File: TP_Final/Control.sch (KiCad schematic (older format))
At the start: 52 parts, among them J101 BG 1x2, J102 BD 1x2, J103 BG 1x2, J104 BG 1x3, J105 Poste 1x4, J106 Poste 2x4, J107 Poste 2x3, K101 EC2-3NU, K102 EC2-3NU, K103 EC2-3NU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

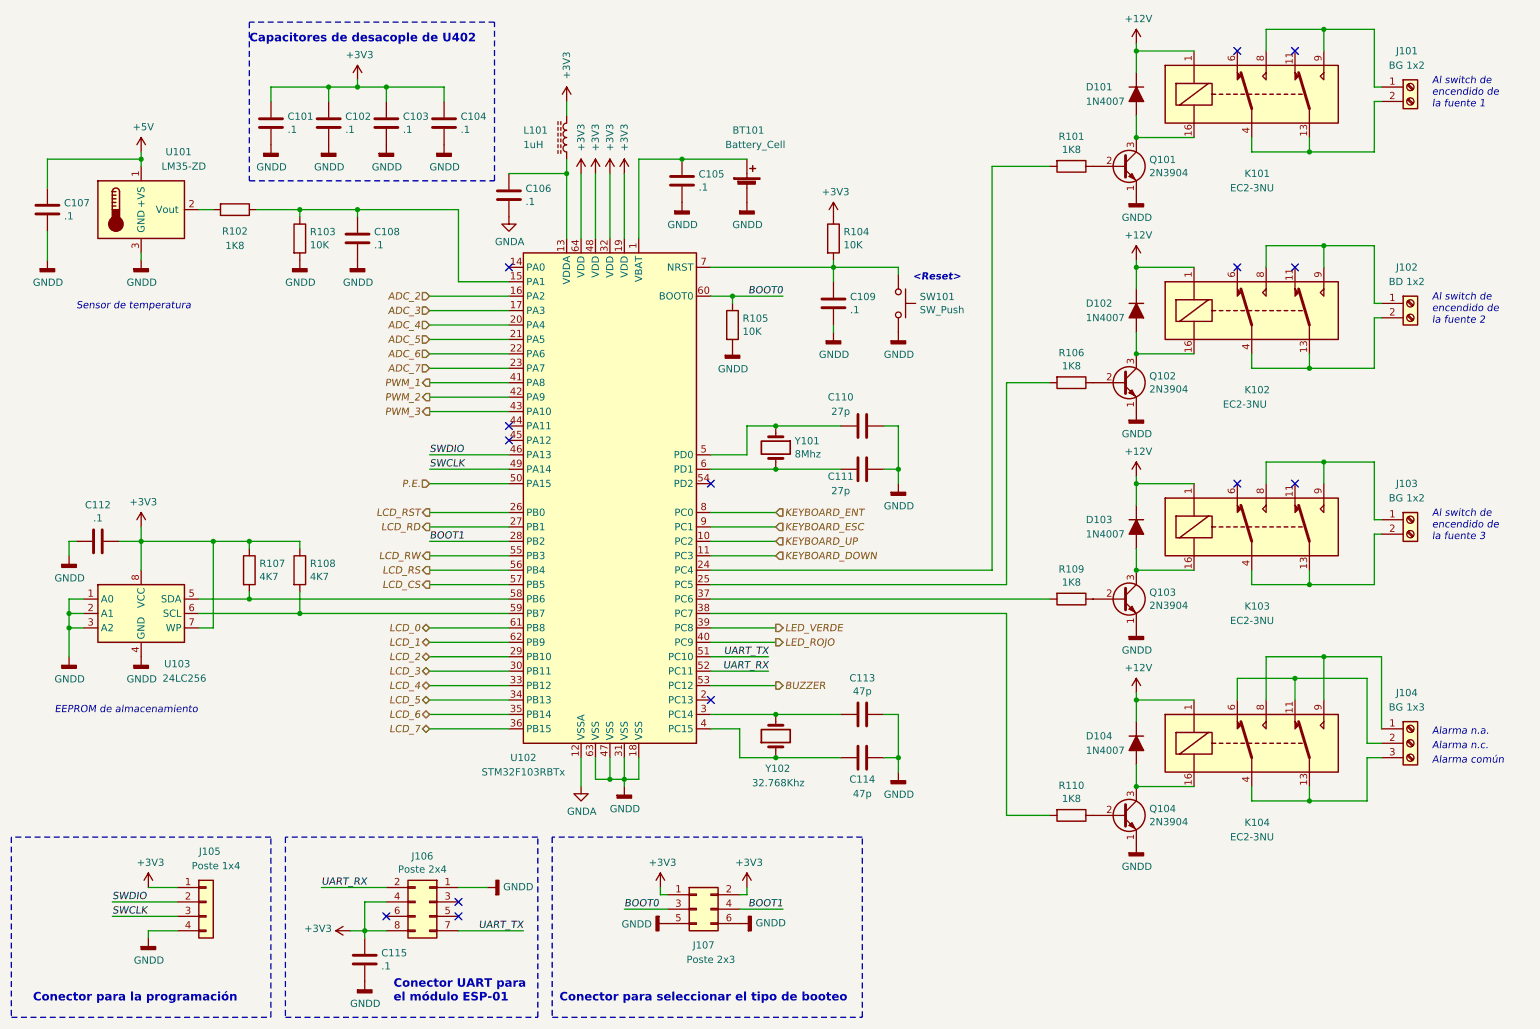
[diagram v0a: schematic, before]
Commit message: se agregan descripciones a componentes del esquemático
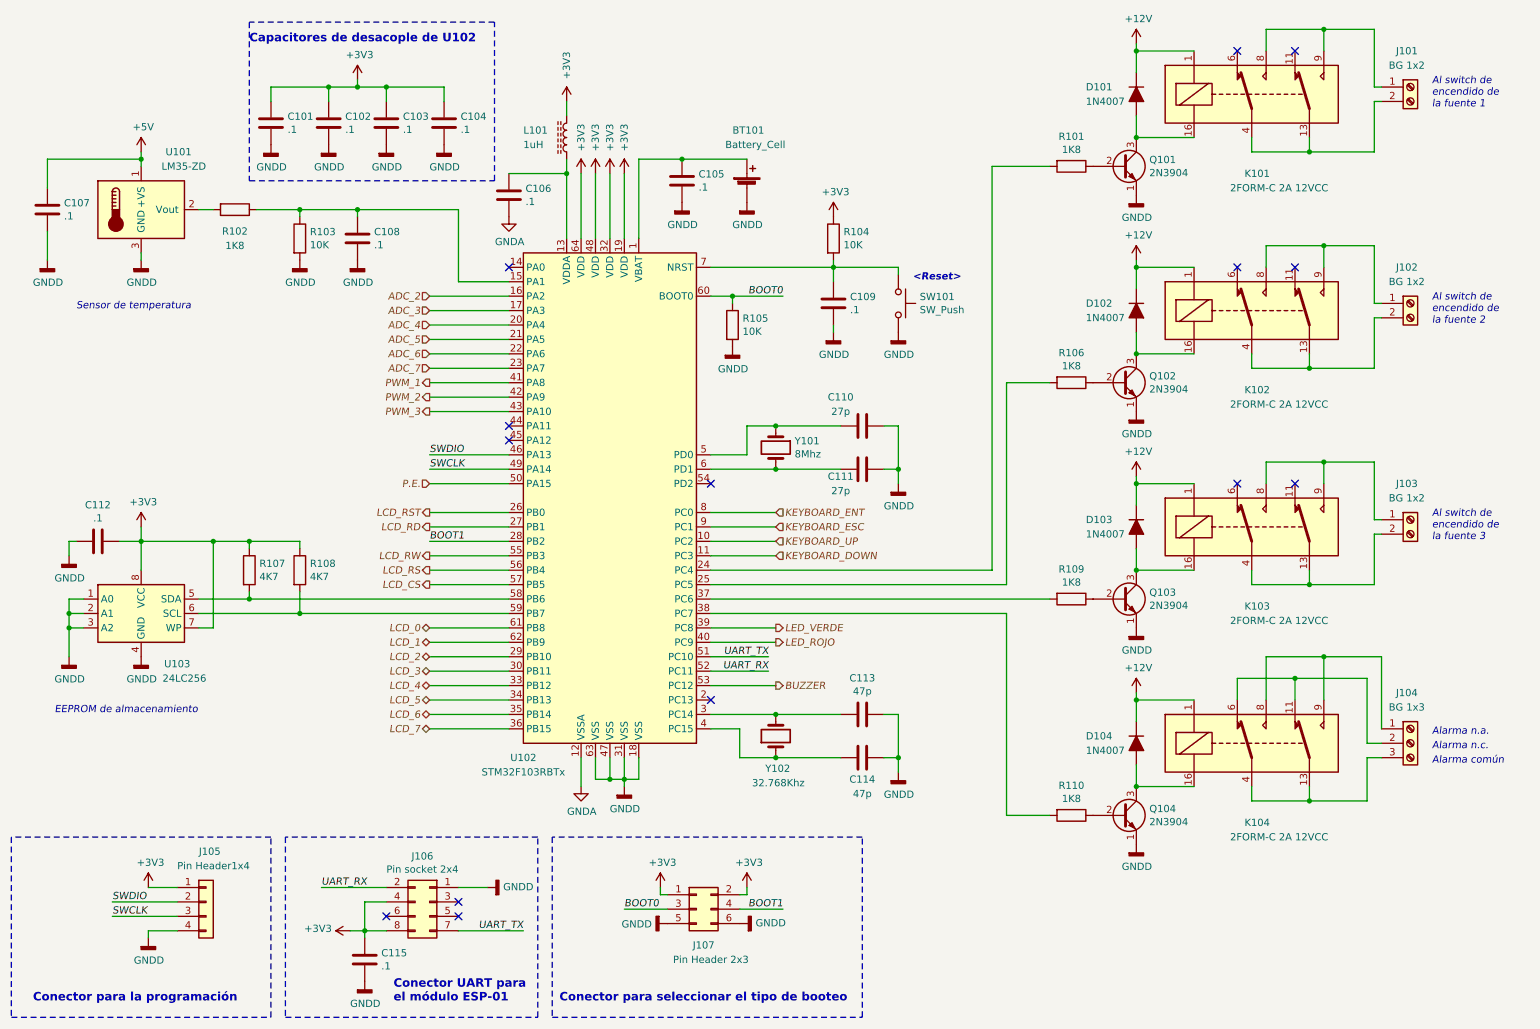
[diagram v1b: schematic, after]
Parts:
- J101: Description (none) -> Bloque de terminales de tornillo PCB; Elemon part (none) -> BO5811874; Eleon part BO5811874 -> (none); Manufac. (none) -> XINYA
- J102: value BD 1x2 -> BG 1x2; Description (none) -> Bloque de terminales de tornillo PCB; Manufac. (none) -> XINYA
- J103, J104: Description (none) -> Bloque de terminales de tornillo PCB; Manufac. (none) -> XINYA
- J105: value Poste 1x4 -> Pin Header1x4
- J106: value Poste 2x4 -> Pin socket 2x4
- J107: value Poste 2x3 -> Pin Header 2x3
- K101, K102, K103, K104: value EC2-3NU -> 2FORM-C 2A 12VCC; Description (none) -> 2FORM-C 2A 12VCC P/CI DIP BC3-12H (20.5x10x11.8MM); Elemon part RE4550956 -> RE4550960; Manufact. (none) -> HANDOUK
- U101: Descripction (none) -> precision integrated-circuit temperature; Manufac. (none) -> Texas
- U102: Description (none) -> Medium-density performance line ARM®-based 32-bit MCU; Manufac. (none) -> ST
- U103: Description (none) -> 256K I2C™ CMOS Serial EEPROM; Manufac. (none) -> Microchip
- Y101: Description (none) -> Cristal 8Mhz, HC-49US, low profile, 20pF capaciadad de carga; Manufac. (none) -> ECS Inc.
- Y102: footprint Crystal:Crystal_AT310_D3.0mm_L10.0mm_Horizontal_1EP_style2 -> Crystal:Crystal_C26-LF_D2.1mm_L6.5mm_Horizontal_1EP_style2; Description (none) -> 32.768 kHz LOW FREQUENCY SMD CRYSTAL; Elemon part OS9009150 -> OS9009152; Manufac. (none) -> CQ
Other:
- note added: "Capacitores de desacople de U102"
- note removed: "Capacitores de desacople de U402"

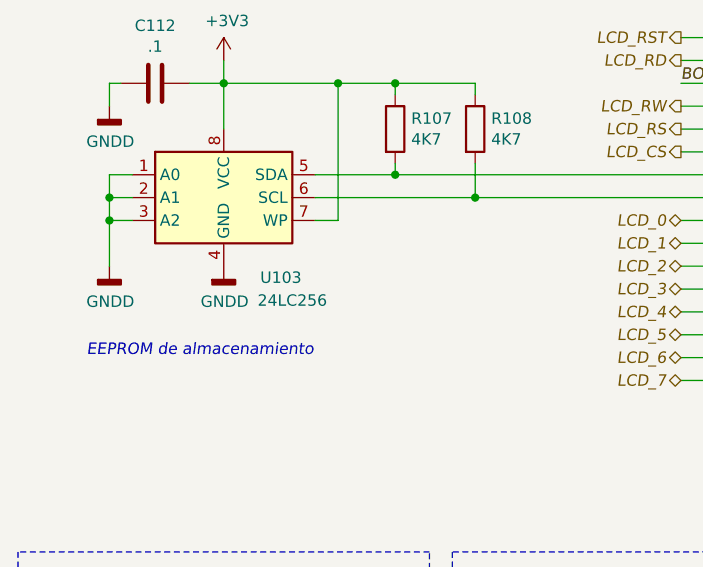
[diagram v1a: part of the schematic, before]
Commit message: Se avanza con el ruteo del PCB
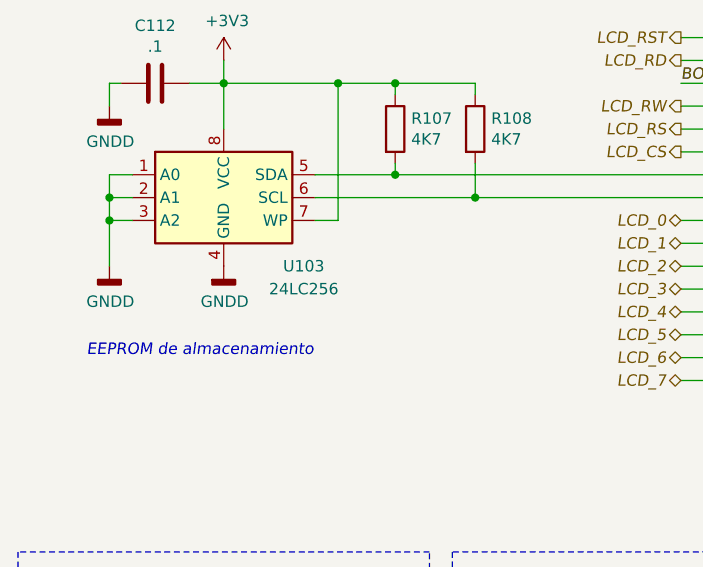
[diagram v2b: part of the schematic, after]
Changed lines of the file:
@@
 U 1 1 60512CA9
 P 1650 4700
-F 0 "U103" H 1900 4350 50  0000 C CNN
-F 1 "24LC256" H 1950 4250 50  0000 C CNN
+F 0 "U103" H 2000 4400 50  0000 C CNN
+F 1 "24LC256" H 2000 4300 50  0000 C CNN
 F 2 "Package_SO:SOIC-8_3.9x4.9mm_P1.27mm" H 1650 4700 50  0001 C CNN
 F 3 "http://ww1.microchip.com/downloads/en/devicedoc/21203m.pdf" H 1650 4700 50  0001 C CNN

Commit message: Agrego agujeros de montaje y fiduciales al esquematico
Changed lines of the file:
@@
 	1    0    0    -1
 $EndComp
+$Comp
+L power:PWR_FLAG #FLG0101
+U 1 1 60755B35
+P 4200 1575
+F 0 "#FLG0101" H 4200 1650 50  0001 C CNN
+F 1 "PWR_FLAG" H 4200 1748 50  0001 C CNN
+F 2 "" H 4200 1575 50  0001 C CNN
+F 3 "~" H 4200 1575 50  0001 C CNN
+	1    4200 1575
+	1    0    0    -1
+$EndComp
+Wire Wire Line
+	4200 1575 4200 1650
+Connection ~ 4200 1650
+$Comp
+L power:PWR_FLAG #FLG0102
+U 1 1 607750BD
+P 5400 1400
+F 0 "#FLG0102" H 5400 1475 50  0001 C CNN
+F 1 "PWR_FLAG" H 5400 1573 50  0000 C CNN
+F 2 "" H 5400 1400 50  0001 C CNN
+F 3 "~" H 5400 1400 50  0001 C CNN
+	1    5400 1400
+	1    0    0    -1
+$EndComp
+Wire Wire Line
+	5400 1550 5400 1400
+$Comp
+L power:PWR_FLAG #FLG0103
+U 1 1 6079705F
+P 8950 5250
+F 0 "#FLG0103" H 8950 5325 50  0001 C CNN
+F 1 "PWR_FLAG" H 8950 5423 50  0000 C CNN
+F 2 "" H 8950 5250 50  0001 C CNN
+F 3 "~" H 8950 5250 50  0001 C CNN
+	1    8950 5250
+	1    0    0    -1
+$EndComp
+Wire Wire Line
+	8950 5250 8950 5300
+Connection ~ 8950 5300
+$Comp
+L power:PWR_FLAG #FLG0104
+U 1 1 607BC1BB
+P 1650 3075
+F 0 "#FLG0104" H 1650 3150 50  0001 C CNN
+F 1 "PWR_FLAG" H 1650 3248 50  0000 C CNN
+F 2 "" H 1650 3075 50  0001 C CNN
+F 3 "~" H 1650 3075 50  0001 C CNN
+	1    1650 3075
+	1    0    0    -1
+$EndComp
+$Comp
+L power:GNDD #PWR0234
+U 1 1 607BCA0E
+P 1650 3175
+F 0 "#PWR0234" H 1650 2925 50  0001 C CNN
+F 1 "GNDD" H 1654 3020 50  0000 C CNN
+F 2 "" H 1650 3175 50  0001 C CNN
+F 3 "" H 1650 3175 50  0001 C CNN
+	1    1650 3175
+	1    0    0    -1
+$EndComp
+Wire Wire Line
+	1650 3175 1650 3075
 $EndSCHEMATC

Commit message: Se cambio huella del portapilas y se completo el relleno de cobre
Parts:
- BT101: footprint Battery:BatteryHolder_Keystone_3001_1x12mm -> Battery:BatteryHolder_Keystone_3034_1x20mm
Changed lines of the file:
@@
 F 0 "BT101" H 5750 2150 50  0000 L CNN
 F 1 "Battery_Cell" H 5700 2050 50  0000 L CNN
-F 2 "Battery:BatteryHolder_Keystone_3001_1x12mm" V 5850 1810 50  0001 C CNN
+F 2 "Battery:BatteryHolder_Keystone_3034_1x20mm" V 5850 1810 50  0001 C CNN
 F 3 "~" V 5850 1810 50  0001 C CNN
 F 4 "36-2997-ND" H 5850 1750 50  0001 C CNN "Digikey part"

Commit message: Correccion power flag y digikey part
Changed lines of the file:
@@
 Wire Wire Line
 	5400 1550 5400 1400
-$Comp
-L power:PWR_FLAG #FLG0103
-U 1 1 6079705F
-P 8950 5250
-F 0 "#FLG0103" H 8950 5325 50  0001 C CNN
-F 1 "PWR_FLAG" H 8950 5423 50  0000 C CNN
-F 2 "" H 8950 5250 50  0001 C CNN
-F 3 "~" H 8950 5250 50  0001 C CNN
-	1    8950 5250
-	1    0    0    -1
-$EndComp
-Wire Wire Line
-	8950 5250 8950 5300
-Connection ~ 8950 5300
-$Comp
-L power:PWR_FLAG #FLG0104
-U 1 1 607BC1BB
-P 1650 3075
-F 0 "#FLG0104" H 1650 3150 50  0001 C CNN
-F 1 "PWR_FLAG" H 1650 3248 50  0000 C CNN
-F 2 "" H 1650 3075 50  0001 C CNN
-F 3 "~" H 1650 3075 50  0001 C CNN
-	1    1650 3075
-	1    0    0    -1
-$EndComp
-$Comp
-L power:GNDD #PWR0234
-U 1 1 607BCA0E
-P 1650 3175
-F 0 "#PWR0234" H 1650 2925 50  0001 C CNN
-F 1 "GNDD" H 1654 3020 50  0000 C CNN
-F 2 "" H 1650 3175 50  0001 C CNN
-F 3 "" H 1650 3175 50  0001 C CNN
-	1    1650 3175
-	1    0    0    -1
-$EndComp
-Wire Wire Line
-	1650 3175 1650 3075
 $EndSCHEMATC
